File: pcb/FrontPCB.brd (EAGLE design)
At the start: 128.4 x 25.1 mm, 0 parts

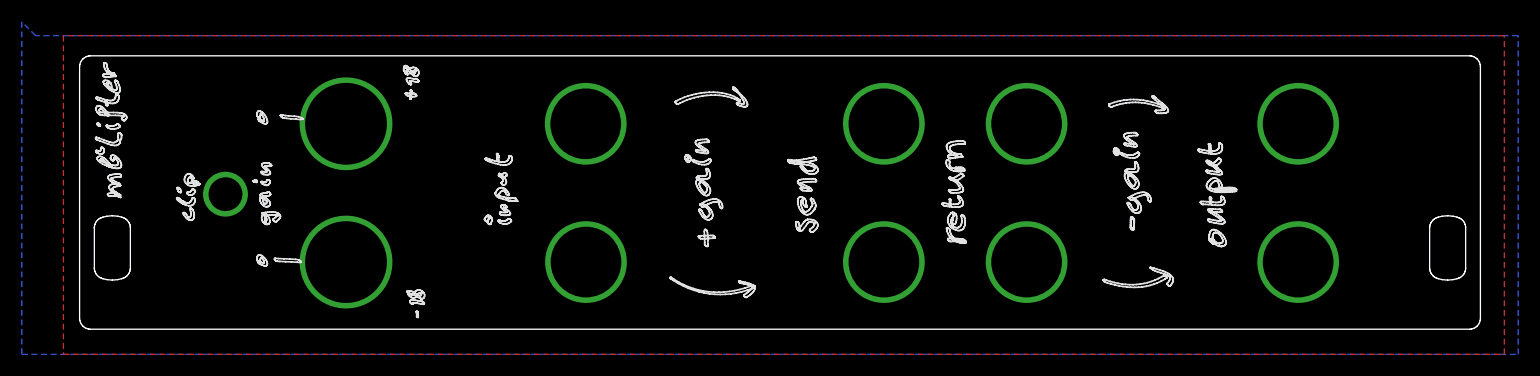
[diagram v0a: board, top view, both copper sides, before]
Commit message: increased pot drill 9mm/355mil
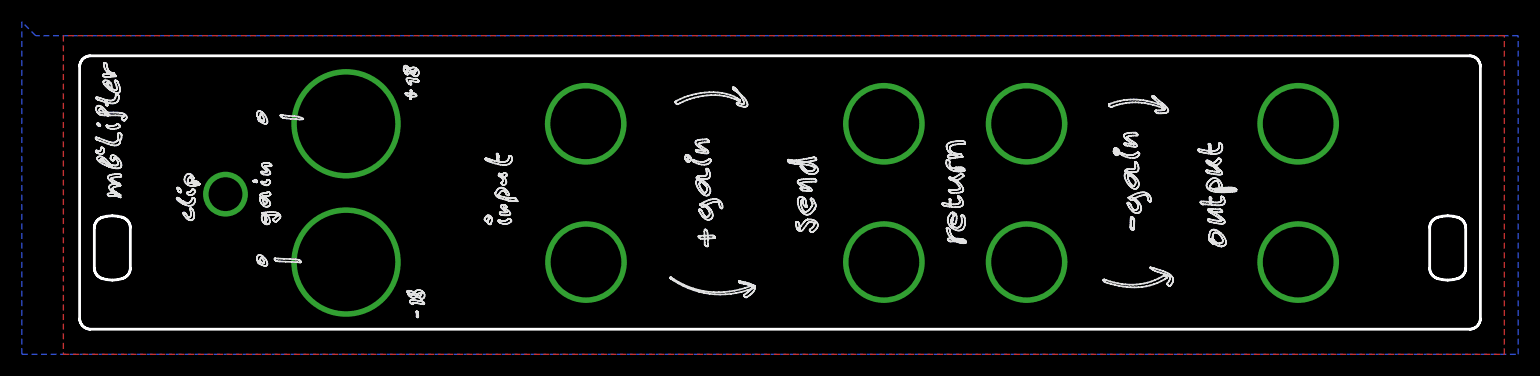
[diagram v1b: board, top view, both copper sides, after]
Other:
- outline, holes or cut-outs redrawn
